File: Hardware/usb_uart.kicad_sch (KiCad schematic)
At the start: 13 parts, among them J2 USB_C_Receptacle_USB2.0, J3 USB_A, U4 CP2102N-Axx-xQFN28

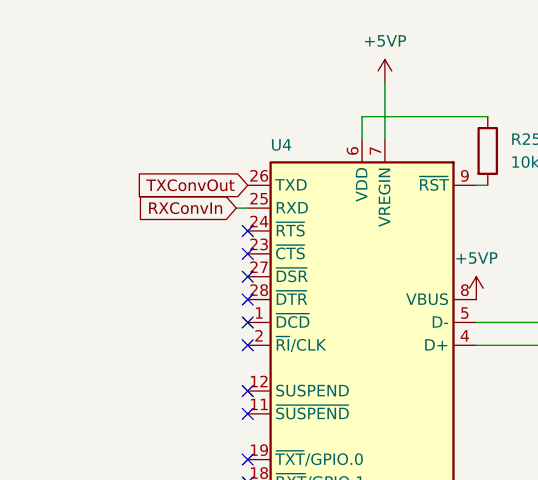
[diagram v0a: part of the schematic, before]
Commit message: added testpoint for TX/RX and updated readme
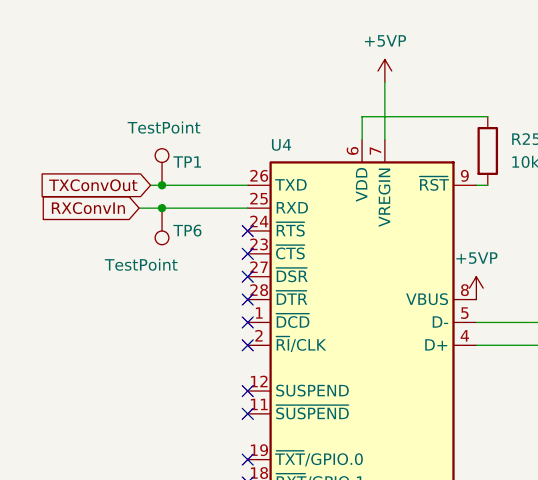
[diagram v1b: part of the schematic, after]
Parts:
- added TP1, TP6: TestPoint, TestPoint:TestPoint_THTPad_D1.0mm_Drill0.5mm, symbol Connector:TestPoint
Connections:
- net RXConvIn: now also TP6.1
- net TXConvOut: now also TP1.1
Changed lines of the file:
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@@
   (junction (at 165.735 78.74) (diameter 0) (color 0 0 0 0)
   )
+  (junction (at 81.28 63.5) (diameter 0) (color 0 0 0 0)
+  )
   (junction (at 140.335 78.74) (diameter 0) (color 0 0 0 0)
   )
@@
   )
   (junction (at 127.635 55.88) (diameter 0) (color 0 0 0 0)
+  )
+  (junction (at 81.28 60.96) (diameter 0) (color 0 0 0 0)
   )
   (junction (at 147.955 48.26) (diameter 0) (color 0 0 0 0)
@@
     (stroke (width 0) (type default))
   )
+  (wire (pts (xy 81.28 60.96) (xy 90.805 60.96))
+    (stroke (width 0) (type default))
+  )
   (wire (pts (xy 165.735 73.66) (xy 165.735 76.2))
     (stroke (width 0) (type default))
@@
     (stroke (width 0) (type default))
   )
+  (wire (pts (xy 80.01 60.96) (xy 81.28 60.96))
+    (stroke (width 0) (type default))
+  )
   (wire (pts (xy 137.795 55.88) (xy 147.955 55.88))
     (stroke (width 0) (type default))
   )
+  (wire (pts (xy 81.28 63.5) (xy 90.805 63.5))
+    (stroke (width 0) (type default))
+  )
   (wire (pts (xy 117.475 53.34) (xy 103.505 53.34))
     (stroke (width 0) (type default))
@@
     (stroke (width 0) (type default))
   )
-  (wire (pts (xy 89.535 63.5) (xy 90.805 63.5))
+  (wire (pts (xy 78.74 63.5) (xy 81.28 63.5))
     (stroke (width 0) (type default))
   )
@@
     )
   )
-  (global_label "TXConvOut" (shape input) (at 90.805 60.96 180) (fields_autoplaced)
+  (global_label "TXConvOut" (shape input) (at 80.01 60.96 180) (fields_autoplaced)
     (effects (font (size 1.27 1.27)) (justify right))
-    (property "Intersheetrefs" "${INTERSHEET_REFS}" (at 77.9019 60.96 0)
+    (property "Intersheetrefs" "${INTERSHEET_REFS}" (at 67.1069 60.96 0)
       (effects (font (size 1.27 1.27)) (justify right) hide)
     )
@@
     )
   )
-  (global_label "RXConvIn" (shape input) (at 89.535 63.5 180) (fields_autoplaced)
+  (global_label "RXConvIn" (shape input) (at 78.74 63.5 180) (fields_autoplaced)
     (effects (font (size 1.27 1.27)) (justify right))
-    (property "Intersheetrefs" "${INTERSHEET_REFS}" (at 77.7809 63.5 0)
+    (property "Intersheetrefs" "${INTERSHEET_REFS}" (at 66.9859 63.5 0)
       (effects (font (size 1.27 1.27)) (justify right) hide)
     )
@@
     (pin "2")
     (instances
-      (project "H616_devboard"
+      (project "kryptokrona-mini-miner"
         (path "/44f68964-8d75-4db0-b784-705712e148bc/95399e0d-575a-4500-9429-e4d55ac775b9"
           (reference "R21") (unit 1)
@@
     (pin "1")
     (instances
-      (project "H616_devboard"
+      (project "kryptokrona-mini-miner"
         (path "/44f68964-8d75-4db0-b784-705712e148bc/95399e0d-575a-4500-9429-e4d55ac775b9"
           (reference "#PWR095") (unit 1)
@@
     (pin "1")
     (instances
-      (project "H616_devboard"
+      (project "kryptokrona-mini-miner"
         (path "/44f68964-8d75-4db0-b784-705712e148bc/95399e0d-575a-4500-9429-e4d55ac775b9"
           (reference "#PWR010") (unit 1)
@@
     )
   )
+  (symbol (lib_id "Connector:TestPoint") (at 81.28 60.96 0) (unit 1)
+    (in_bom yes) (on_board yes) (dnp no)
+    (property "Reference" "TP1" (at 82.55 58.42 0)
+      (effects (font (size 1.27 1.27)) (justify left))
+    )
+    (property "Value" "TestPoint" (at 77.47 54.61 0)
+      (effects (font (size 1.27 1.27)) (justify left))
+    )
+    (property "Footprint" "TestPoint:TestPoint_THTPad_D1.0mm_Drill0.5mm" (at 86.36 60.96 0)
+      (effects (font (size 1.27 1.27)) hide)
+    )
+    (property "Datasheet" "~" (at 86.36 60.96 0)
+      (effects (font (size 1.27 1.27)) hide)
+    )
+    (pin "1")
+    (instances
+      (project "kryptokrona-mini-miner"
+        (path "/44f68964-8d75-4db0-b784-705712e148bc/95399e0d-575a-4500-9429-e4d55ac775b9"
+          (reference "TP1") (unit 1)
+        )
+      )
+    )
+  )
   (symbol (lib_id "power:GND") (at 103.505 121.92 0) (mirror y) (unit 1)
     (in_bom yes) (on_board yes) (dnp no)
@@
     (pin "1")
     (instances
-      (project "H616_devboard"
+      (project "kryptokrona-mini-miner"
         (path "/44f68964-8d75-4db0-b784-705712e148bc/95399e0d-575a-4500-9429-e4d55ac775b9"
           (reference "#PWR093") (unit 1)
@@
     (pin "2")
     (instances
-      (project "H616_devboard"
+      (project "kryptokrona-mini-miner"
         (path "/44f68964-8d75-4db0-b784-705712e148bc/95399e0d-575a-4500-9429-e4d55ac775b9"
           (reference "D3") (unit 1)
@@
     (pin "S1")
     (instances
-      (project "H616_devboard"
+      (project "kryptokrona-mini-miner"
         (path "/44f68964-8d75-4db0-b784-705712e148bc/95399e0d-575a-4500-9429-e4d55ac775b9"
           (reference "J2") (unit 1)
@@
     (pin "2")
     (instances
-      (project "H616_devboard"
+      (project "kryptokrona-mini-miner"
         (path "/44f68964-8d75-4db0-b784-705712e148bc/95399e0d-575a-4500-9429-e4d55ac775b9"
           (reference "R22") (unit 1)
@@
     (pin "9")
     (instances
-      (project "H616_devboard"
+      (project "kryptokrona-mini-miner"
         (path "/44f68964-8d75-4db0-b784-705712e148bc/95399e0d-575a-4500-9429-e4d55ac775b9"
           (reference "U4") (unit 1)
@@
     (pin "1")
     (instances
-      (project "H616_devboard"
+      (project "kryptokrona-mini-miner"
         (path "/44f68964-8d75-4db0-b784-705712e148bc/95399e0d-575a-4500-9429-e4d55ac775b9"
           (reference "#PWR096") (unit 1)
@@
     (pin "5")
     (instances
-      (project "H616_devboard"
+      (project "kryptokrona-mini-miner"
         (path "/44f68964-8d75-4db0-b784-705712e148bc/95399e0d-575a-4500-9429-e4d55ac775b9"
           (reference "J3") (unit 1)
@@
     (pin "1")
     (instances
-      (project "H616_devboard"
+      (project "kryptokrona-mini-miner"
         (path "/44f68964-8d75-4db0-b784-705712e148bc/95399e0d-575a-4500-9429-e4d55ac775b9"
           (reference "#PWR089") (unit 1)
@@
     (pin "1")
     (instances
-      (project "H616_devboard"
+      (project "kryptokrona-mini-miner"
         (path "/44f68964-8d75-4db0-b784-705712e148bc/95399e0d-575a-4500-9429-e4d55ac775b9"
           (reference "#PWR090") (unit 1)
@@
     (pin "1")
     (instances
-      (project "H616_devboard"
+      (project "kryptokrona-mini-miner"
         (path "/44f68964-8d75-4db0-b784-705712e148bc/95399e0d-575a-4500-9429-e4d55ac775b9"
           (reference "#PWR087") (unit 1)
@@
     (pin "2")
     (instances
-      (project "H616_devboard"
+      (project "kryptokrona-mini-miner"
         (path "/44f68964-8d75-4db0-b784-705712e148bc/95399e0d-575a-4500-9429-e4d55ac775b9"
           (reference "C66") (unit 1)
@@
     (pin "1")
     (instances
-      (project "H616_devboard"
+      (project "kryptokrona-mini-miner"
         (path "/44f68964-8d75-4db0-b784-705712e148bc/95399e0d-575a-4500-9429-e4d55ac775b9"
           (reference "#PWR092") (unit 1)
@@
     (pin "1")
     (instances
-      (project "H616_devboard"
+      (project "kryptokrona-mini-miner"
         (path "/44f68964-8d75-4db0-b784-705712e148bc/95399e0d-575a-4500-9429-e4d55ac775b9"
           (reference "#PWR094") (unit 1)
@@
     (pin "1")
     (instances
-      (project "H616_devboard"
+      (project "kryptokrona-mini-miner"
         (path "/44f68964-8d75-4db0-b784-705712e148bc/95399e0d-575a-4500-9429-e4d55ac775b9"
           (reference "#PWR097") (unit 1)
@@
     (pin "1")
     (instances
-      (project "H616_devboard"
+      (project "kryptokrona-mini-miner"
         (path "/44f68964-8d75-4db0-b784-705712e148bc/95399e0d-575a-4500-9429-e4d55ac775b9"
           (reference "#PWR088") (unit 1)
@@
     (pin "2")
     (instances
-      (project "H616_devboard"
+      (project "kryptokrona-mini-miner"
         (path "/44f68964-8d75-4db0-b784-705712e148bc/95399e0d-575a-4500-9429-e4d55ac775b9"
           (reference "C67") (unit 1)
@@
     (pin "2")
     (instances
-      (project "H616_devboard"
+      (project "kryptokrona-mini-miner"
         (path "/44f68964-8d75-4db0-b784-705712e148bc/95399e0d-575a-4500-9429-e4d55ac775b9"
           (reference "C69") (unit 1)
@@
     (pin "2")
     (instances
-      (project "H616_devboard"
+      (project "kryptokrona-mini-miner"
         (path "/44f68964-8d75-4db0-b784-705712e148bc/95399e0d-575a-4500-9429-e4d55ac775b9"
           (reference "C68") (unit 1)
@@
     (pin "2")
     (instances
-      (project "H616_devboard"
+      (project "kryptokrona-mini-miner"
         (path "/44f68964-8d75-4db0-b784-705712e148bc/95399e0d-575a-4500-9429-e4d55ac775b9"
           (reference "D4") (unit 1)
@@
     (pin "2")
     (instances
-      (project "H616_devboard"
+      (project "kryptokrona-mini-miner"
         (path "/44f68964-8d75-4db0-b784-705712e148bc/95399e0d-575a-4500-9429-e4d55ac775b9"
           (reference "C65") (unit 1)
@@
     (pin "1")
     (instances
-      (project "H616_devboard"
+      (project "kryptokrona-mini-miner"
         (path "/44f68964-8d75-4db0-b784-705712e148bc/95399e0d-575a-4500-9429-e4d55ac775b9"
           (reference "#PWR086") (unit 1)
+        )
+      )
+    )
+  )
+  (symbol (lib_id "Connector:TestPoint") (at 81.28 63.5 180) (unit 1)
+    (in_bom yes) (on_board yes) (dnp no)
+    (property "Reference" "TP6" (at 82.55 66.04 0)
+      (effects (font (size 1.27 1.27)) (justify right))
+    )
+    (property "Value" "TestPoint" (at 74.93 69.85 0)
+      (effects (font (size 1.27 1.27)) (justify right))
+    )
+    (property "Footprint" "TestPoint:TestPoint_THTPad_D1.0mm_Drill0.5mm" (at 76.2 63.5 0)
+      (effects (font (size 1.27 1.27)) hide)
+    )
+    (property "Datasheet" "~" (at 76.2 63.5 0)
+      (effects (font (size 1.27 1.27)) hide)
+    )
+    (pin "1")
+    (instances
+      (project "kryptokrona-mini-miner"
+        (path "/44f68964-8d75-4db0-b784-705712e148bc/95399e0d-575a-4500-9429-e4d55ac775b9"
+          (reference "TP6") (unit 1)
         )
       )
@@
     (pin "2")
     (instances
-      (project "H616_devboard"
+      (project "kryptokrona-mini-miner"
         (path "/44f68964-8d75-4db0-b784-705712e148bc/95399e0d-575a-4500-9429-e4d55ac775b9"
           (reference "R25") (unit 1)
